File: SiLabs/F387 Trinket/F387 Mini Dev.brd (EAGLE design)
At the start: 25.4 x 15.2 mm, 17 parts, among them J1 1X7, J2 1X7, J3 1X1, SW1 SPST.B3U-1000P(M)-B, U1 C8051F387, U2 SP0503BAHTG

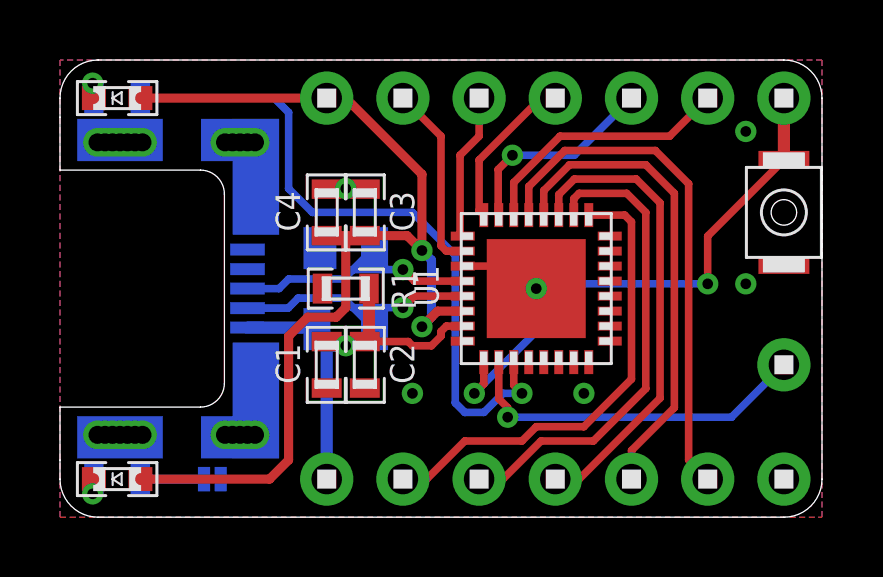
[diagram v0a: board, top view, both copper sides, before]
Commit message: Redid Trinket clone to add FTDI header capabilities Replaced USB ESD protection IC with tinier variant. All passives are now 0402 sized (oh boy...) Power domains should be fixed as well
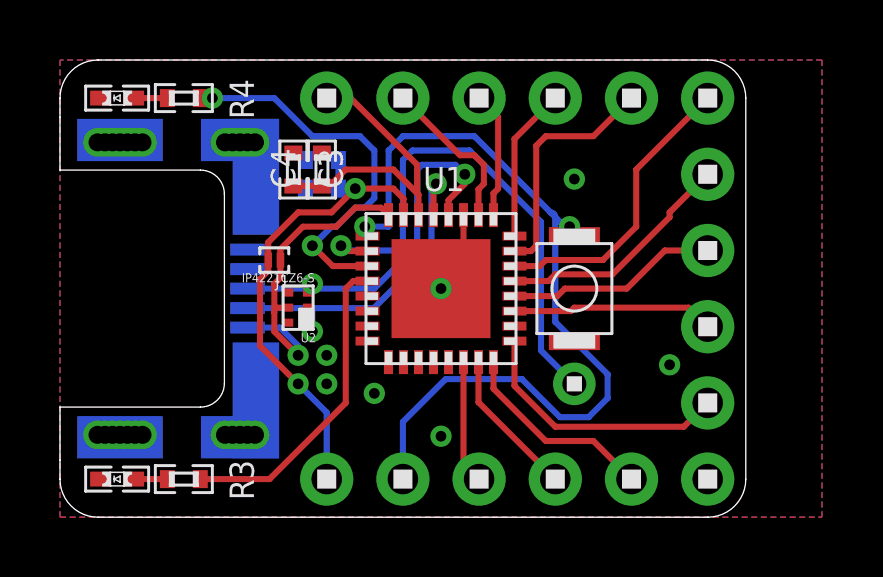
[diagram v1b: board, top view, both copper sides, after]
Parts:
- removed J2: 1X7, headers(.1in):1X7
- removed J3: 1X1, headers(.1in):1X1
- removed J4: (no value), solderjumper:2.MED.PASTE
- removed R1: 100k, standardparts:0603
- added H1, H3: 1X5, headers(.1in):1X5
- added H2: 1X6, headers(.1in):1X6
- added H4: 1X1, headers(2mm):1X1
- C1, C2, C3, C4, R3, R4: device standardparts:0603 -> standardparts:0402
- D1, D2: device standardparts:0603.LED -> standardparts:0402.LED
- J1: value 1X7 -> (none); device headers(.1in):1X7 -> solderjumper:2.SML
- SW1: value SPST.B3U-1000P(M)-B -> SPST.B3U-1000P(M); device omron:B3U-1000P(M)-B -> omron:B3U-1000P(M)
- U2: value SP0503BAHTG -> IP4221CZ6-S; device littlefuse:SOT143 -> nxp:DFN1410-6
- moved J1 7.51 mm to (7.14, 8.57), turned to 180 degrees
- moved SW1 7.43 mm to (17.1, 7.62)
- moved C2 6.97 mm to (8.73, 11.9), flipped to the bottom, turned to 0 degrees
- moved C1 5.88 mm to (8.73, 11.0), flipped to the bottom, turned to 0 degrees
- moved U1 3.18 mm to (12.7, 7.62), turned to 270 degrees
- moved C3 2.78 mm to (7.78, 11.6)
- moved R3 2.22 mm to (4.13, 1.27), flipped to the top, turned to 0 degrees
- moved R4 2.22 mm to (4.13, 14.0), flipped to the top, turned to 0 degrees
- moved U2 1.71 mm to (7.94, 6.99), flipped to the top, turned to 180 degrees
- moved C4 1.44 mm to (8.73, 11.6)
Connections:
- removed net N$3: D2.P$2, R4.1
- removed net P1.0: J1.3, U1.26
- new net 5.0V: J1.1, U1.8, U2.5, USB.1
- new net P1.2: H3.1, U1.24
- new net P1.3: H3.2, U1.23
- new net P1.4: H3.3, U1.22
- new net P2.6: R3.2, U1.12
- net !RST: now also H3.4; no longer J2.7
- net 3.3V: now also H1.1; no longer D1.P$1, D2.P$1, J2.1
- net C2D: now also H4.1; no longer J3.1
- net D+: now also U2.3; no longer U2.2
- net D-: now also U2.1; no longer U2.3
- net GND: now also D1.P$2, D2.P$2, H2.6, U2.2; no longer J1.7, J4.1, R1.2, U1.8, U2.1, USB.4
- net N$1: now also D1.P$1; no longer D1.P$2
- net N$2: now also D2.P$1, R4.1; no longer J4.2, R3.2
- net P0.0: now also H1.2; no longer J2.2
- net P0.1: now also H1.3; no longer J2.3
- net P0.2: now also H1.4; no longer J2.4
- net P0.3: now also H1.5; no longer J2.5
- net P0.4: now also H2.1; no longer J2.6
- net P0.5: now also H2.2; no longer J1.6
- net P0.6: now also H2.3; no longer J1.5
- net P0.7: now also H2.4; no longer J1.4
- net P1.1: now also H2.5; no longer J1.2
- net VIN: now also H3.5, J1.2; no longer J1.1, R1.1, U2.4, USB.1
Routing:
- net 3.3V: track 34.8 -> 10.3 mm, vias 2 -> 0
- net P1.0: track 16.0 -> 0.00 mm
- net 5.0V: track 0.00 -> 11.0 mm, vias 0 -> 1
- net !RST: track 17.7 -> 28.6 mm
- net P2.6: track 0.00 -> 10.5 mm
- net P2.7: track 22.8 -> 12.9 mm, vias 1 -> 2
- net P0.5: track 17.3 -> 8.01 mm
- net P0.7: track 15.7 -> 6.75 mm
- net P0.6: track 16.0 -> 7.07 mm
- net P1.1: track 15.8 -> 8.83 mm
- net P1.2: track 0.00 -> 6.74 mm
- net C2D: track 11.9 -> 17.5 mm
- net P1.3: track 0.00 -> 4.96 mm
- net P1.4: track 0.00 -> 4.12 mm
- net D+: track 8.61 -> 12.7 mm, vias 1 -> 2
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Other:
- board size 25.4 x 15.2 mm -> 22.9 x 15.2 mm
- board text added: "5v"
- board text removed: "P2.7"
- board text removed: "PWR"
- board text removed: "VBUS"
